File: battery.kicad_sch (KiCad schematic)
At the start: 43 parts, among them IC2 XB8089D, J1 USB_C_Receptacle, SW3 SW_SPST, U3 BQ24092DGQR, U4 TPS61085DGKR, U5 TPS259621DDAT

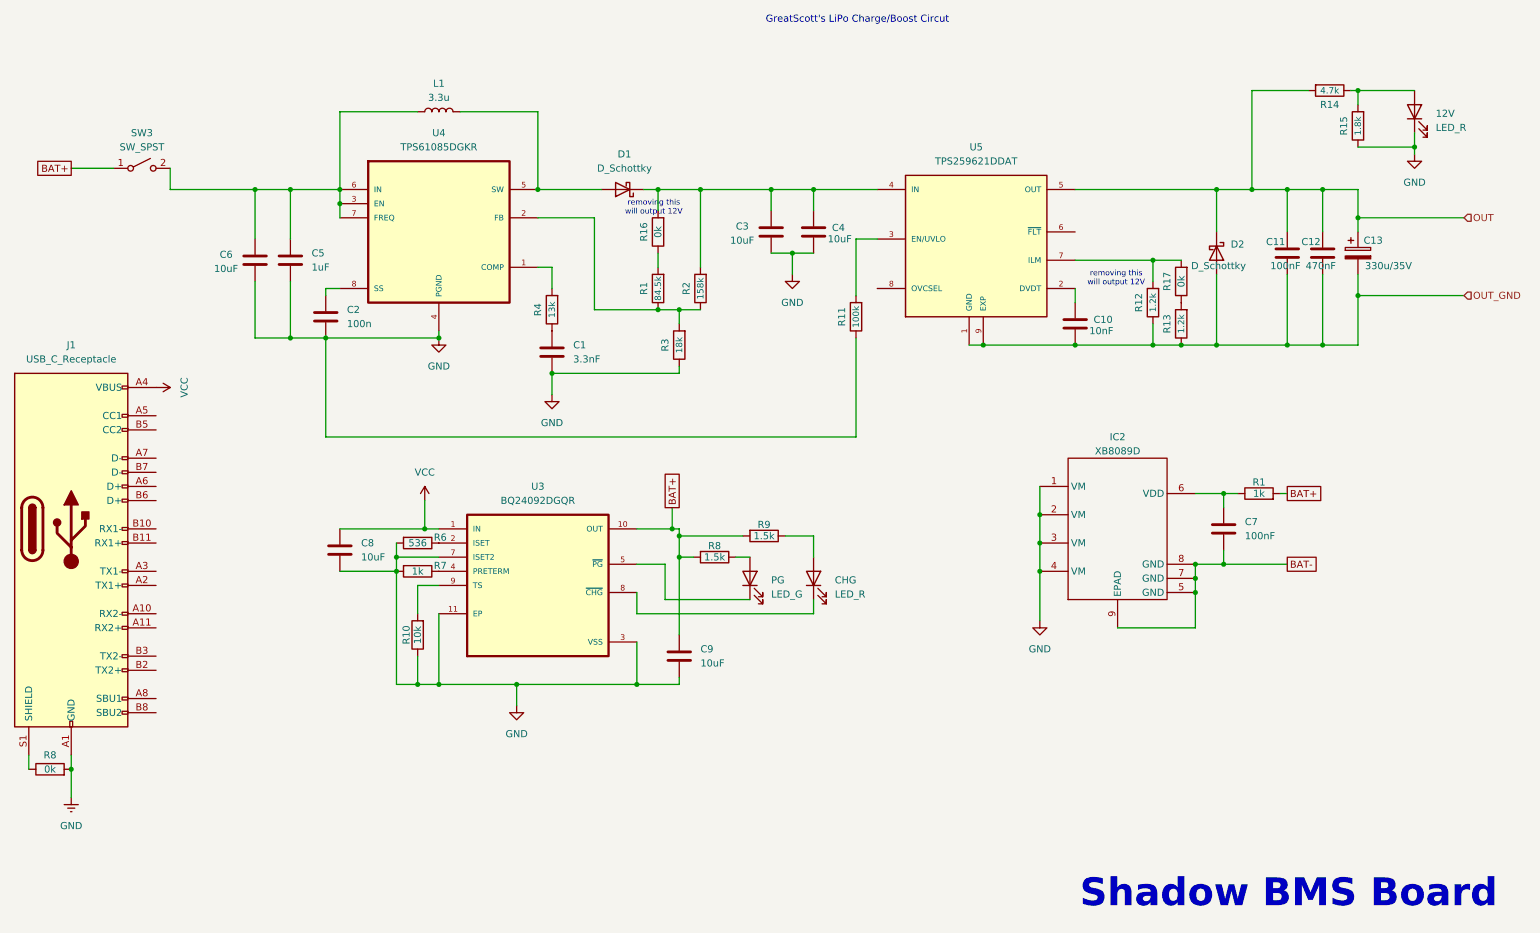
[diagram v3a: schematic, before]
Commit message: Add new lipo charger to pcb
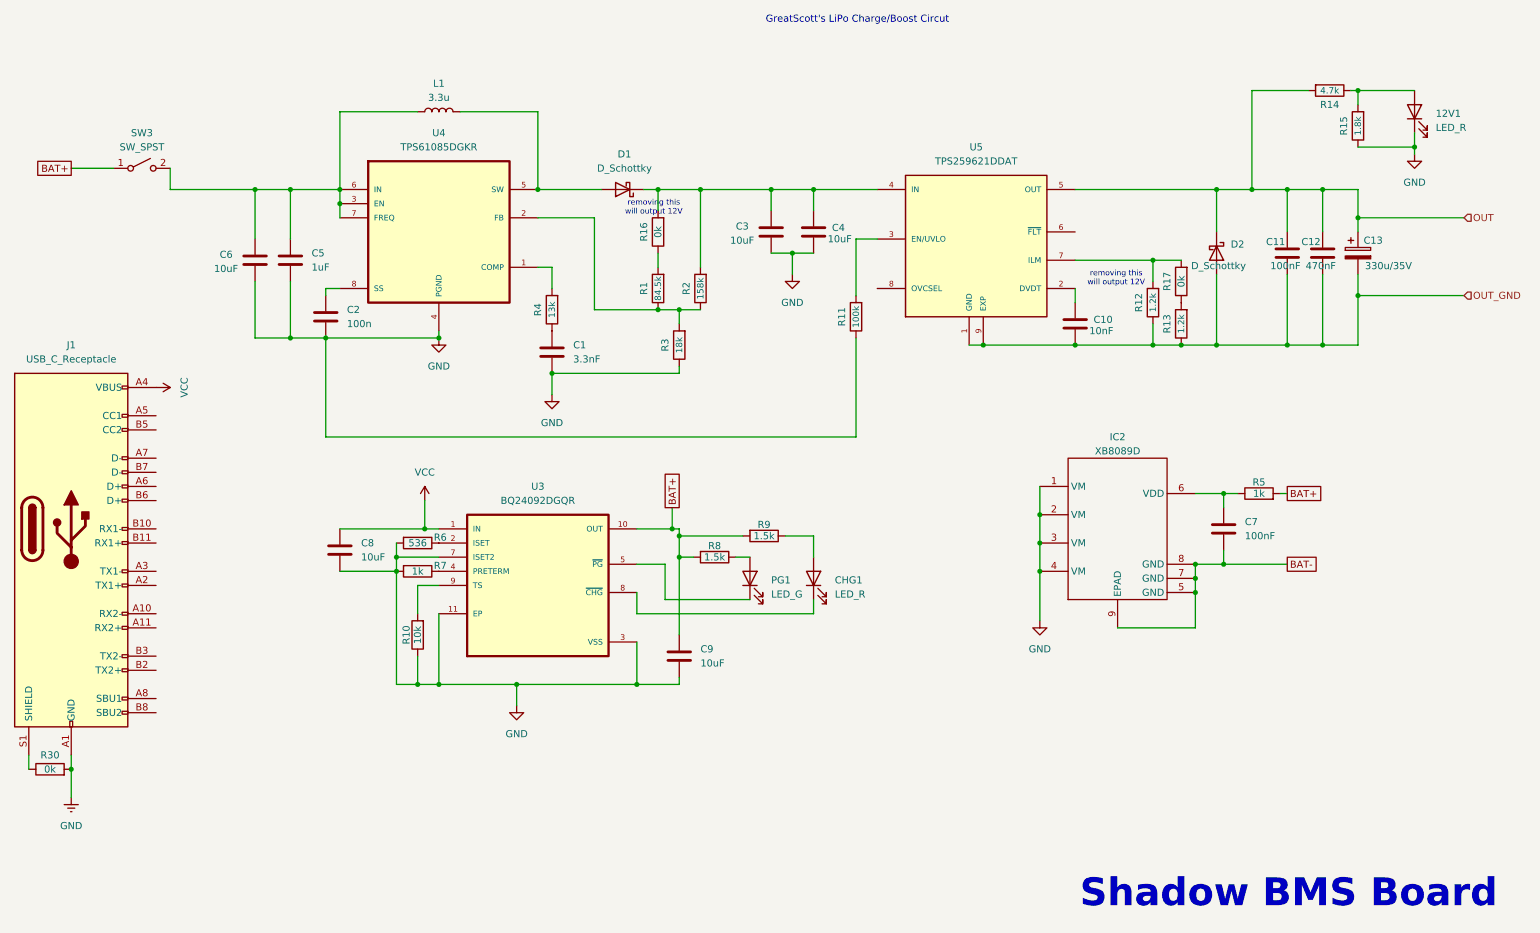
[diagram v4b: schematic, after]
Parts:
- 12V1: renamed from 12V; footprint (none) -> LED_SMD:LED_1206_3216Metric
- C1, C10, C11, C12, C13, C2, C3, C4, C5, C6, C7, C8, C9: footprint (none) -> Capacitor_SMD:C_1206_3216Metric
- CHG1: renamed from CHG; footprint (none) -> LED_SMD:LED_1206_3216Metric
- D1, D2: footprint (none) -> Diode_SMD:D_1206_3216Metric
- IC2: footprint ProLib_pcs_2025-01-25:SOIC-8_L5.0-W4.0-P1.27-LS6.0-BL-EP2.0 -> XB8089D:XB8089D
- L1: footprint (none) -> Inductor_SMD:L_7.3x7.3_H4.5
- PG1: renamed from PG; footprint (none) -> LED_SMD:LED_1206_3216Metric
- R10, R6, R7, R8, R9: footprint (none) -> Resistor_SMD:R_1206_3216Metric
- R5: renamed from R1; footprint (none) -> Resistor_SMD:R_1206_3216Metric
- U5: footprint TPS259621DDAT:IC_TPS259621DDAT -> TPS259621:IC_TPS259621DDAT
- renumbered R8 to R30
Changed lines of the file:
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@@
 			)
 		)
-		(property "Footprint" ""
+		(property "Footprint" "Capacitor_SMD:C_1206_3216Metric"
 			(at 249.8852 60.96 0)
 			(effects
@@
 			)
 		)
-		(property "Footprint" ""
+		(property "Footprint" "Capacitor_SMD:C_1206_3216Metric"
 			(at 232.1052 110.49 0)
 			(effects
@@
 		(dnp no)
 		(fields_autoplaced yes)
-		(property "Reference" "12V"
+		(property "Reference" "12V1"
 			(at 269.24 32.0674 90)
 			(effects
@@
 			)
 		)
-		(property "Footprint" ""
+		(property "Footprint" "LED_SMD:LED_1206_3216Metric"
 			(at 265.43 31.75 0)
 			(effects
@@
 			(project "shadow"
 				(path "/3c2fce68-ba60-4bda-a294-ddd60ff77106/353b67ec-a1cb-4a2a-a9c5-6f61edaa503f"
-					(reference "12V")
+					(reference "12V1")
 					(unit 1)
 				)
@@
 			)
 		)
-		(property "Footprint" ""
+		(property "Footprint" "Resistor_SMD:R_1206_3216Metric"
 			(at 148.59 106.172 90)
 			(effects
@@
 		(dnp no)
 		(fields_autoplaced yes)
-		(property "Reference" "CHG"
+		(property "Reference" "CHG1"
 			(at 161.29 115.8874 90)
 			(effects
@@
 			)
 		)
-		(property "Footprint" ""
+		(property "Footprint" "LED_SMD:LED_1206_3216Metric"
 			(at 157.48 115.57 0)
 			(effects
@@
 			(project "shadow"
 				(path "/3c2fce68-ba60-4bda-a294-ddd60ff77106/353b67ec-a1cb-4a2a-a9c5-6f61edaa503f"
-					(reference "CHG")
+					(reference "CHG1")
 					(unit 1)
 				)
@@
 			)
 		)
-		(property "Footprint" ""
+		(property "Footprint" "Capacitor_SMD:C_1206_3216Metric"
 			(at 243.5352 60.96 0)
 			(effects
@@
 			)
 		)
-		(property "Footprint" ""
+		(property "Footprint" "Diode_SMD:D_1206_3216Metric"
 			(at 123.19 45.72 0)
 			(effects
@@
 			)
 		)
-		(property "Footprint" ""
+		(property "Footprint" "Inductor_SMD:L_7.3x7.3_H4.5"
 			(at 90.17 31.75 0)
 			(effects
@@
 			)
 		)
-		(property "Footprint" ""
+		(property "Footprint" "Resistor_SMD:R_1206_3216Metric"
 			(at 86.36 112.522 90)
 			(effects
@@
 			)
 		)
-		(property "Footprint" ""
+		(property "Footprint" "Capacitor_SMD:C_1206_3216Metric"
 			(at 158.4452 57.15 0)
 			(effects
@@
 		(on_board yes)
 		(dnp no)
-		(property "Reference" "R8"
+		(property "Reference" "R30"
 			(at 20.32 147.32 90)
 			(effects
@@
 			(project "shadow"
 				(path "/3c2fce68-ba60-4bda-a294-ddd60ff77106/353b67ec-a1cb-4a2a-a9c5-6f61edaa503f"
-					(reference "R8")
+					(reference "R30")
 					(unit 1)
 				)
@@
 			)
 		)
-		(property "Footprint" ""
+		(property "Footprint" "Capacitor_SMD:C_1206_3216Metric"
 			(at 70.8152 72.39 0)
 			(effects
@@
 			)
 		)
-		(property "Footprint" ""
+		(property "Footprint" "Capacitor_SMD:C_1206_3216Metric"
 			(at 64.4652 62.23 0)
 			(effects
@@
 			)
 		)
-		(property "Footprint" ""
+		(property "Footprint" "Capacitor_SMD:C_1206_3216Metric"
 			(at 73.3552 114.3 0)
 			(effects
@@
 		(dnp no)
 		(fields_autoplaced yes)
-		(property "Reference" "PG"
+		(property "Reference" "PG1"
 			(at 149.86 115.8874 90)
 			(effects
@@
 			)
 		)
-		(property "Footprint" ""
+		(property "Footprint" "LED_SMD:LED_1206_3216Metric"
 			(at 146.05 115.57 0)
 			(effects
@@
 			(project ""
 				(path "/3c2fce68-ba60-4bda-a294-ddd60ff77106/353b67ec-a1cb-4a2a-a9c5-6f61edaa503f"
-					(reference "PG")
+					(reference "PG1")
 					(unit 1)
 				)
@@
 			)
 		)
-		(property "Footprint" ""
+		(property "Footprint" "Diode_SMD:D_1206_3216Metric"
 			(at 229.87 57.15 0)
 			(effects
@@
 		(on_board yes)
 		(dnp no)
-		(property "Reference" "R1"
+		(property "Reference" "R5"
 			(at 237.49 98.298 90)
 			(effects
@@
 			)
 		)
-		(property "Footprint" ""
+		(property "Footprint" "Resistor_SMD:R_1206_3216Metric"
 			(at 237.49 102.108 90)
 			(effects
@@
 			(project ""
 				(path "/3c2fce68-ba60-4bda-a294-ddd60ff77106/353b67ec-a1cb-4a2a-a9c5-6f61edaa503f"
-					(reference "R1")
+					(reference "R5")
 					(unit 1)
 				)
@@
 			)
 		)
-		(property "Footprint" ""
+		(property "Footprint" "Capacitor_SMD:C_1206_3216Metric"
 			(at 205.4352 73.66 0)
 			(effects
@@
 			)
 		)
-		(property "Footprint" ""
+		(property "Footprint" "Resistor_SMD:R_1206_3216Metric"
 			(at 139.7 109.982 90)
 			(effects
@@
 			)
 		)
-		(property "Footprint" "TPS259621DDAT:IC_TPS259621DDAT"
+		(property "Footprint" "TPS259621:IC_TPS259621DDAT"
 			(at 188.214 83.058 0)
 			(effects
@@
 			)
 		)
-		(property "Footprint" ""
+		(property "Footprint" "Capacitor_SMD:C_1206_3216Metric"
 			(at 111.4552 78.74 0)
 			(effects
@@
 			)
 		)
-		(property "Footprint" ""
+		(property "Footprint" "Capacitor_SMD:C_1206_3216Metric"
 			(at 58.1152 62.23 0)
 			(effects
@@
 			)
 		)
-		(property "Footprint" ""
+		(property "Footprint" "Capacitor_SMD:C_1206_3216Metric"
 			(at 134.3152 133.35 0)
 			(effects
@@
 			)
 		)
-		(property "Footprint" ""
+		(property "Footprint" "Resistor_SMD:R_1206_3216Metric"
 			(at 86.36 107.442 90)
 			(effects
@@
 			)
 		)
-		(property "Footprint" "ProLib_pcs_2025-01-25:SOIC-8_L5.0-W4.0-P1.27-LS6.0-BL-EP2.0"
+		(property "Footprint" "XB8089D:XB8089D"
 			(at 212.09 106.68 0)
 			(effects
@@
 			)
 		)
-		(property "Footprint" ""
+		(property "Footprint" "Capacitor_SMD:C_1206_3216Metric"
 			(at 256.2352 60.96 0)
 			(effects
@@
 			)
 		)
-		(property "Footprint" ""
+		(property "Footprint" "Capacitor_SMD:C_1206_3216Metric"
 			(at 150.8252 57.15 0)
 			(effects
@@
 			)
 		)
-		(property "Footprint" ""
+		(property "Footprint" "Resistor_SMD:R_1206_3216Metric"
 			(at 88.138 125.73 90)
 			(effects

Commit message: a lot of work on pcb
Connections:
- net VCC: no longer names the net of C8.1, J1.A4 (VBUS), J1.A9 (VBUS), J1.B4 (VBUS), J1.B9 (VBUS), U3.1 (IN)
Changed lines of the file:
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@@
 	(wire
 		(pts
+			(xy 57.15 81.28) (xy 57.15 101.6)
+		)
+		(stroke
+			(width 0)
+			(type default)
+		)
+	)
+	(wire
+		(pts
 			(xy 104.14 138.43) (xy 104.14 134.62)
 		)
@@
 	(wire
 		(pts
+			(xy 39.37 81.28) (xy 57.15 81.28)
+		)
+		(stroke
+			(width 0)
+			(type default)
+		)
+	)
+	(wire
+		(pts
 			(xy 242.57 53.34) (xy 242.57 45.72)
 		)
@@
 	(wire
 		(pts
+			(xy 57.15 101.6) (xy 87.63 101.6)
+		)
+		(stroke
+			(width 0)
+			(type default)
+		)
+	)
+	(wire
+		(pts
 			(xy 110.49 78.74) (xy 110.49 82.55)
 		)
@@
 		)
 	)
-	(global_label "BAT+"
+	(hierarchical_label "BAT+"
 		(shape passive)
-		(at 242.57 100.33 0)
+		(at 132.08 102.87 90)
 		(fields_autoplaced yes)
 		(effects
@@
 			(justify left)
 		)
-		(property "Intersheetrefs" "${INTERSHEET_REFS}"
-			(at 249.3425 100.33 0)
-			(effects
-				(font
-					(size 1.27 1.27)
-				)
-				(justify left)
-				(hide yes)
-			)
-		)
 	)
-	(global_label "BAT-"
+	(hierarchical_label "BAT+"
 		(shape passive)
-		(at 242.57 113.03 0)
+		(at 24.13 41.91 180)
 		(fields_autoplaced yes)
 		(effects
@@
 				(size 1.27 1.27)
 			)
-			(justify left)
-		)
-		(property "Intersheetrefs" "${INTERSHEET_REFS}"
-			(at 249.3425 113.03 0)
-			(effects
-				(font
-					(size 1.27 1.27)
-				)
-				(justify left)
-				(hide yes)
-			)
+			(justify right)
 		)
 	)
-	(global_label "BAT+"
+	(hierarchical_label "BAT+"
 		(shape passive)
-		(at 24.13 41.91 180)
+		(at 242.57 100.33 0)
 		(fields_autoplaced yes)
 		(effects
@@
 				(size 1.27 1.27)
 			)
-			(justify right)
-		)
-		(property "Intersheetrefs" "${INTERSHEET_REFS}"
-			(at 17.3575 41.91 0)
-			(effects
-				(font
-					(size 1.27 1.27)
-				)
-				(justify right)
-				(hide yes)
-			)
+			(justify left)
 		)
 	)
-	(global_label "BAT+"
+	(hierarchical_label "BAT-"
 		(shape passive)
-		(at 132.08 102.87 90)
+		(at 242.57 113.03 0)
 		(fields_autoplaced yes)
 		(effects
@@
 			(justify left)
 		)
-		(property "Intersheetrefs" "${INTERSHEET_REFS}"
-			(at 132.08 96.0975 90)
-			(effects
-				(font
-					(size 1.27 1.27)
-				)
-				(justify left)
-				(hide yes)
-			)
-		)
 	)
 	(hierarchical_label "OUT"
@@
 	)
 	(symbol
-		(lib_id "power:VCC")
-		(at 87.63 101.6 0)
-		(unit 1)
-		(exclude_from_sim no)
-		(in_bom yes)
-		(on_board yes)
-		(dnp no)
-		(fields_autoplaced yes)
-		(property "Reference" "#PWR07"
-			(at 87.63 105.41 0)
-			(effects
-				(font
-					(size 1.27 1.27)
-				)
-				(hide yes)
-			)
-		)
-		(property "Value" "VCC"
-			(at 87.63 96.52 0)
-			(effects
-				(font
-					(size 1.27 1.27)
-				)
-			)
-		)
-		(property "Footprint" ""
-			(at 87.63 101.6 0)
-			(effects
-				(font
-					(size 1.27 1.27)
-				)
-				(hide yes)
-			)
-		)
-		(property "Datasheet" ""
-			(at 87.63 101.6 0)
-			(effects
-				(font
-					(size 1.27 1.27)
-				)
-				(hide yes)
-			)
-		)
-		(property "Description" "Power symbol creates a global label with name \"VCC\""
-			(at 87.63 101.6 0)
-			(effects
-				(font
-					(size 1.27 1.27)
-				)
-				(hide yes)
-			)
-		)
-		(pin "1"
-		)
-		(instances
-			(project "shadow"
-				(path "/3c2fce68-ba60-4bda-a294-ddd60ff77106/353b67ec-a1cb-4a2a-a9c5-6f61edaa503f"
-					(reference "#PWR07")
-					(unit 1)
-				)
-			)
-		)
-	)
-	(symbol
 		(lib_id "Device:D_Schottky")
 		(at 123.19 45.72 180)
@@
 					(unit 1)
 				)
-			)
-		)
-	)
-	(symbol
-		(lib_id "power:VCC")
-		(at 39.37 81.28 270)
-		(unit 1)
-		(exclude_from_sim no)
-		(in_bom yes)
-		(on_board yes)
-		(dnp no)
-		(fields_autoplaced yes)
-		(property "Reference" "#PWR06"
-			(at 35.56 81.28 0)
-			(effects
-				(font
-					(size 1.27 1.27)
-				)
-				(hide yes)
-			)
-		)
-		(property "Value" "VCC"
-			(at 44.45 81.28 0)
-			(effects
-				(font
-					(size 1.27 1.27)
-				)
-			)
-		)
-		(property "Footprint" ""
-			(at 39.37 81.28 0)
-			(effects
-				(font
-					(size 1.27 1.27)
-				)
-				(hide yes)
-			)
-		)
-		(property "Datasheet" ""
-			(at 39.37 81.28 0)
-			(effects
-				(font
-					(size 1.27 1.27)
-				)
-				(hide yes)
-			)
-		)
-		(property "Description" "Power symbol creates a global label with name \"VCC\""
-			(at 39.37 81.28 0)
-			(effects
-				(font
-					(size 1.27 1.27)
-				)
-				(hide yes)
-			)
-		)
-		(pin "1"
-		)
-		(instances
-			(project ""
-				(path "/3c2fce68-ba60-4bda-a294-ddd60ff77106/353b67ec-a1cb-4a2a-a9c5-6f61edaa503f"
-					(reference "#PWR06")
-					(unit 1)
-				)

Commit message: Update to new cap footprint
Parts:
- C13: footprint Capacitor_SMD:C_1206_3216Metric -> Capacitor_THT:CP_Radial_D10.0mm_P5.00mm
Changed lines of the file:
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@@
 			)
 		)
-		(property "Footprint" "Capacitor_SMD:C_1206_3216Metric"
+		(property "Footprint" "Capacitor_THT:CP_Radial_D10.0mm_P5.00mm"
 			(at 256.2352 60.96 0)
 			(effects

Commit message: finish pcb
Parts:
- removed R30: 0k, Resistor_SMD:R_0201_0603Metric, symbol Device:R
- removed SW3: SW_SPST, Button_Switch_THT:SW_DIP_SPSTx01_Slide_9.78x4.72mm_W7.62mm_P2.54mm, symbol Switch:SW_SPST
- added SW3: ~, Switch:SW-TH_K3-2235D-F1, symbol ProLib_pcs_2025-01-26:K3-2235D-F1
- J1: footprint Connector_USB:USB_C_Receptacle_GCT_USB4085 -> USB_C:TYPE-C-SMD_20009-UCAF001-X; symbol Connector:USB_C_Receptacle -> USB_C:TYPE-C 16PIN L8.35; LCSC Part Name (none) -> Type-C 母 卧贴; Manufacturer (none) -> SHOU HAN(首韩); Manufacturer Part (none) -> TYPE-C 16PIN L8.35; Supplier (none) -> LCSC; Supplier Part (none) -> C5379909
- R1, R11, R12, R13, R14, R15, R16, R17, R2, R3, R4: footprint Resistor_SMD:R_0201_0603Metric -> Resistor_SMD:R_1206_3216Metric
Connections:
- net BAT+: now also SW3.1
- net GND: now also J1.1, J1.2, J1.3, J1.4
- net VBUS: now reaches C8.1, J1.A4 (VBUS), J1.A9 (VBUS), J1.B4 (VBUS), J1.B9 (VBUS), U3.1 (IN)
- net at C5.1, C6.1, L1.1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: now also SW3.4
